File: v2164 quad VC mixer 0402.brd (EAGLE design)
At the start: 39.4 x 14.6 mm, 43 parts, among them IC1 TL072JD, IC2 TL072JD

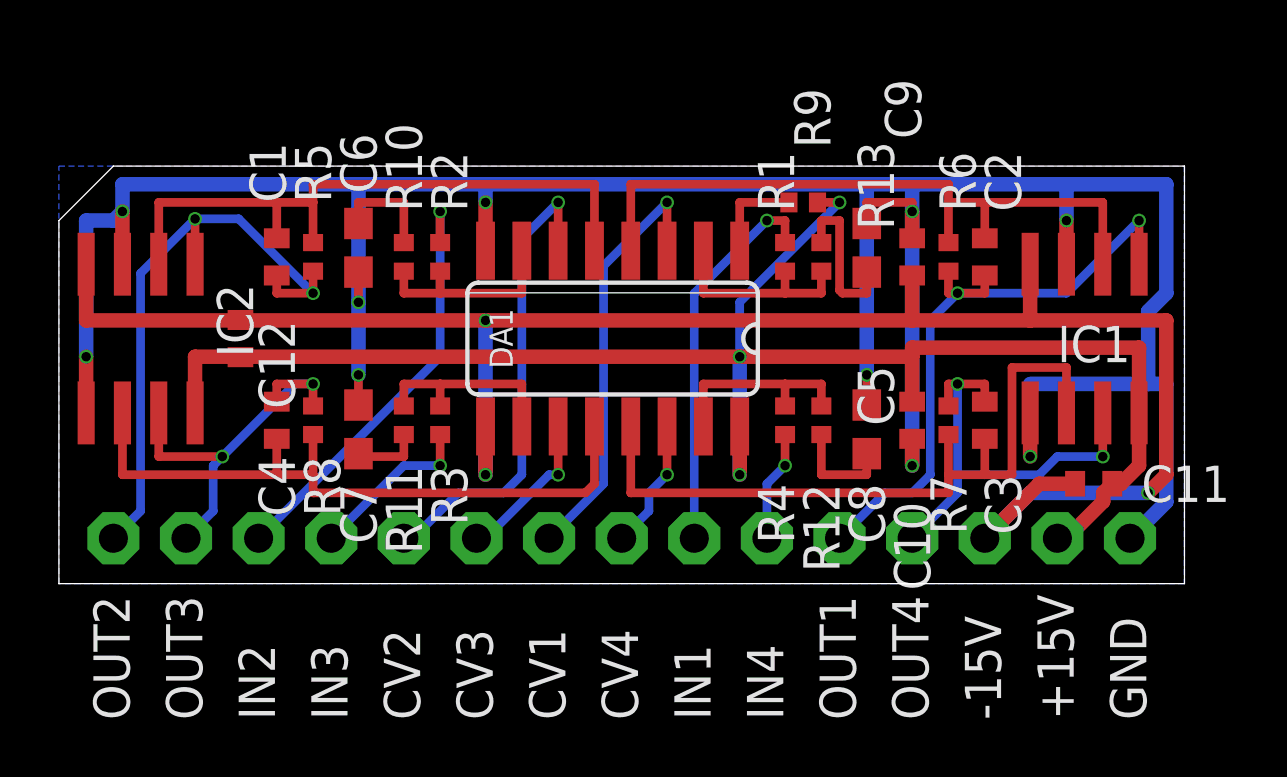
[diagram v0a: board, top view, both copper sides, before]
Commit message: Made mixer and added top labels
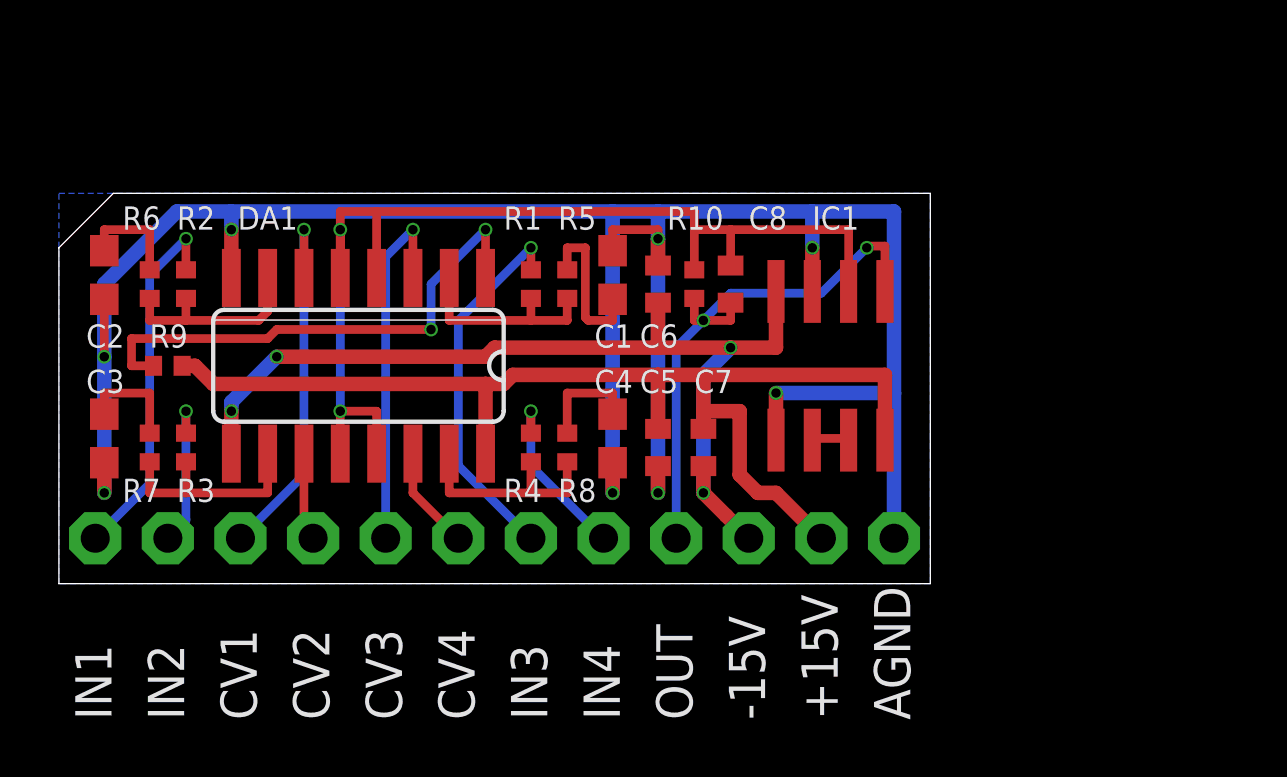
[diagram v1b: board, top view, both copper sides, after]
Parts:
- removed C10, C11, C12, C9: 100nF, rcl:C0402
- removed GND, OUT1, OUT2, OUT3, OUT4: (no value), joakim:MA01N-1J
- removed IC2: TL072JD, joakim:SO08J
- removed R11, R12: 500R, rcl:R0402
- removed R13: 7.5k for A, rcl:R0402
- added AGND, OUT: (no value), joakim:MA01N-1J
- C1, C2, C3, C4: value 100pF -> 560pF; device rcl:C0402 -> rcl:C0603
- C5, C6, C7: value 560pF -> 100nF; device rcl:C0603 -> rcl:C0402
- C8: value 560pF -> 100pF; device rcl:C0603 -> rcl:C0402
- R10: value 500R -> 30k
- R5, R6, R7, R8: value 30k -> 500R
- R9: value 500R -> 7.5k for A
- moved C2 30.8 mm to (1.59, 10.8), turned to 90 degrees
- moved C3 30.8 mm to (1.59, 5.08)
- moved R6 28.0 mm to (3.17, 10.5)
- moved R7 28.0 mm to (3.17, 4.76), turned to 270 degrees
- moved R9 23.2 mm to (3.81, 7.62), turned to 180 degrees
- moved IN1 21.0 mm to (1.27, 1.59)
- moved C7 12.1 mm to (22.5, 4.76), turned to 90 degrees
- moved C1 11.8 mm to (19.4, 10.8)
- moved C4 11.8 mm to (19.4, 5.08)
- moved CV1 10.8 mm to (6.35, 1.59)
- moved C6 10.6 mm to (21.0, 10.5)
- moved R10 10.2 mm to (22.2, 10.5)
- moved C5 10.1 mm to (21.0, 4.76), turned to 90 degrees
- moved DA1 8.94 mm to (10.5, 7.62)
- moved R2 8.94 mm to (4.45, 10.5)
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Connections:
- removed net CV3: CV3.1, DA1.11
- removed net N$3: C3.1, DA1.13, IC1.6, R7.1
- removed net N$7: C1.1, DA1.5, IC2.2, R5.1
- removed net OUT1: C2.2, IC1.1, OUT1.1, R6.2
- removed net OUT2: C1.2, IC2.1, OUT2.1, R5.2
- removed net OUT3: C4.2, IC2.7, OUT3.1, R8.2
- removed net OUT4: C3.2, IC1.7, OUT4.1, R7.2
- new net CV5: CV3.1, DA1.3
- new net OUT: C8.2, IC1.1, OUT.1, R10.2
- net +15V: now also C5.2, C7.2, R9.1; no longer C10.2, C11.2, C12.2, IC2.8, R13.1
- net -15V: now also C6.1, C7.1; no longer C11.1, C12.1, C9.1, IC2.4
- net CV1: now also DA1.6; no longer DA1.3
- net CV2: now also DA1.11; no longer DA1.6
- net GND: now also AGND.1, C1.1, C2.1, C3.1, C4.1, C6.2; no longer C10.1, C6.1, C7.1, C8.1, C9.2, GND.1, IC2.3, IC2.5
- net IN1: now also R2.1; no longer R1.1
- net IN2: now also R3.1; no longer R2.1
- net IN3: now also R1.1; no longer R3.1
- net N$1: now also IC1.6, IC1.7; no longer C4.1, DA1.12, IC2.6, R8.1
- net N$10: now also C2.2, R6.1; no longer C6.2, R10.1
- net N$11: now also C3.2, R7.1; no longer C7.2, R11.1
- net N$12: now also C4.2, R8.1; no longer C8.2, R12.1
- net N$17: now also R5.2; no longer R9.2
- net N$18: now also R6.2; no longer R10.2
- net N$19: now also R7.2; no longer R11.2
- net N$2: now also R9.2; no longer R13.2
- net N$20: now also R8.2; no longer R12.2
- net N$5: now also C8.1, DA1.12, DA1.13, DA1.5, R10.1; no longer C2.1, R6.1
- net N$9: now also C1.2, R5.1; no longer C5.2, R9.1
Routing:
- net -15V: track 67.0 -> 33.8 mm, vias 3 -> 4
- net N$3: track 26.2 -> 0.00 mm
- net N$7: track 23.0 -> 0.00 mm
- net N$1: track 24.1 -> 1.39 mm
- net OUT1: track 22.4 -> 0.00 mm, vias 2 -> 0
- net OUT2: track 21.8 -> 0.00 mm, vias 2 -> 0
- net OUT: track 0.00 -> 19.7 mm, vias 0 -> 2
- net +15V: track 58.5 -> 40.7 mm, vias 3 -> 0
- net GND: track 102.9 -> 86.6 mm, vias 10 -> 8
- net N$5: track 24.3 -> 40.2 mm, vias 0 -> 2
- net OUT4: track 15.6 -> 0.00 mm, vias 2 -> 0
- net N$2: track 3.41 -> 18.3 mm, vias 0 -> 2
- net OUT3: track 14.0 -> 0.00 mm, vias 2 -> 0
- net CV2: track 16.8 -> 3.09 mm, vias 1 -> 0
- net CV5: track 0.00 -> 12.9 mm, vias 0 -> 1
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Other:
- board size 39.4 x 14.6 mm -> 30.5 x 13.7 mm

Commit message: Finished top layer on both boards i think
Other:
- board text added: "3-20"
- board text added: "4VOB"
- board text added: "v1"
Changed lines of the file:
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@@
 <wire x1="30.48" y1="13.6525" x2="30.48" y2="0" width="0" layer="20"/>
 <wire x1="30.48" y1="0" x2="0" y2="0" width="0" layer="20"/>
+<text x="28.575" y="3.81" size="1.016" layer="25" font="vector" rot="R180">4VOB</text>
+<text x="11.43" y="12.3825" size="0.8128" layer="25" font="vector">3-20</text>
+<text x="28.8925" y="12.3825" size="0.8128" layer="25" font="vector">v1</text>
 </plain>
 <attributes>

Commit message: Completed silkscreen and routing on both vca and mixer.
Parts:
- added U$1: (no value), joakim:XONIK_LOGO_20
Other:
- board text added: "+15v"
- board text added: "-15v"
- board text added: "4ch exp mixer"
- board text added: "AGND"
- board text added: "C1"
- board text added: "C2"
- board text added: "C3"
- board text added: "C4"
- board text added: "I1"
- board text added: "I2"
- board text added: "I3"
- board text added: "I4"
- board text added: "O"
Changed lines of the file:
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@@
 <layer number="2" name="Route2" color="16" fill="1" visible="no" active="no"/>
 <layer number="15" name="Route15" color="23" fill="1" visible="no" active="no"/>
-<layer number="16" name="Bottom" color="1" fill="1" visible="yes" active="yes"/>
+<layer number="16" name="Bottom" color="1" fill="1" visible="no" active="yes"/>
 <layer number="17" name="Pads" color="2" fill="1" visible="yes" active="yes"/>
 <layer number="18" name="Vias" color="2" fill="1" visible="yes" active="yes"/>
@@
 <layer number="20" name="Dimension" color="24" fill="1" visible="yes" active="yes"/>
 <layer number="21" name="tPlace" color="7" fill="1" visible="yes" active="yes"/>
-<layer number="22" name="bPlace" color="7" fill="1" visible="yes" active="yes"/>
+<layer number="22" name="bPlace" color="7" fill="1" visible="no" active="yes"/>
 <layer number="23" name="tOrigins" color="15" fill="1" visible="yes" active="yes"/>
-<layer number="24" name="bOrigins" color="15" fill="1" visible="yes" active="yes"/>
+<layer number="24" name="bOrigins" color="15" fill="1" visible="no" active="yes"/>
 <layer number="25" name="tNames" color="7" fill="1" visible="yes" active="yes"/>
-<layer number="26" name="bNames" color="7" fill="1" visible="yes" active="yes"/>
+<layer number="26" name="bNames" color="7" fill="1" visible="no" active="yes"/>
 <layer number="27" name="tValues" color="7" fill="1" visible="no" active="yes"/>
 <layer number="28" name="bValues" color="7" fill="1" visible="no" active="yes"/>
@@
 <layer number="38" name="bTest" color="7" fill="1" visible="no" active="yes"/>
 <layer number="39" name="tKeepout" color="4" fill="11" visible="yes" active="yes"/>
-<layer number="40" name="bKeepout" color="1" fill="11" visible="yes" active="yes"/>
+<layer number="40" name="bKeepout" color="1" fill="11" visible="no" active="yes"/>
 <layer number="41" name="tRestrict" color="4" fill="10" visible="yes" active="yes"/>
-<layer number="42" name="bRestrict" color="1" fill="10" visible="yes" active="yes"/>
+<layer number="42" name="bRestrict" color="1" fill="10" visible="no" active="yes"/>
 <layer number="43" name="vRestrict" color="2" fill="10" visible="no" active="yes"/>
 <layer number="44" name="Drills" color="7" fill="1" visible="no" active="yes"/>
@@
 <layer number="50" name="dxf" color="7" fill="1" visible="no" active="no"/>
 <layer number="51" name="tDocu" color="7" fill="1" visible="yes" active="yes"/>
-<layer number="52" name="bDocu" color="7" fill="1" visible="yes" active="yes"/>
+<layer number="52" name="bDocu" color="7" fill="1" visible="no" active="yes"/>
 <layer number="53" name="tGND_GNDA" color="7" fill="9" visible="no" active="no"/>
 <layer number="54" name="bGND_GNDA" color="1" fill="9" visible="no" active="no"/>
@@
 <text x="11.43" y="12.3825" size="0.8128" layer="25" font="vector">3-20</text>
 <text x="28.8925" y="12.3825" size="0.8128" layer="25" font="vector">v1</text>
+<text x="0.635" y="3.4925" size="1.27" layer="26" font="vector" rot="MR90">I1</text>
+<text x="3.175" y="3.4925" size="1.27" layer="26" font="vector" rot="MR90">I2</text>
+<text x="5.715" y="3.4925" size="1.27" layer="26" font="vector" rot="MR90">C1</text>
+<text x="8.255" y="3.4925" size="1.27" layer="26" font="vector" rot="MR90">C2</text>
+<text x="10.795" y="3.4925" size="1.27" layer="26" font="vector" rot="MR90">C3</text>
+<text x="13.335" y="3.4925" size="1.27" layer="26" font="vector" rot="MR90">C4</text>
+<text x="15.875" y="3.4925" size="1.27" layer="26" font="vector" rot="MR90">I3</text>
+<text x="18.415" y="3.4925" size="1.27" layer="26" font="vector" rot="MR90">I4</text>
+<text x="20.955" y="3.4925" size="1.27" layer="26" font="vector" rot="MR90">O</text>
+<text x="23.495" y="3.4925" size="1.27" layer="26" font="vector" rot="MR90">-15v</text>
+<text x="26.035" y="3.4925" size="1.27" layer="26" font="vector" rot="MR90">+15v</text>
+<text x="28.575" y="3.4925" size="1.27" layer="26" font="vector" rot="MR90">AGND</text>
+<text x="17.145" y="6.35" size="1.27" layer="26" font="vector" rot="MR0">4ch exp mixer</text>
 </plain>
 <attributes>
@@
 </element>
 <element name="CV3" library="joakim" package="MA01N-1J" value="" x="11.43" y="1.5875" smashed="yes" rot="R90">
-<attribute name="NAME" x="12.0015" y="-4.7625" size="1.27" layer="25" ratio="10" rot="R90"/>
 <attribute name="VALUE" x="14.351" y="-0.9525" size="1.27" layer="27" ratio="10" rot="R90"/>
 </element>
 <element name="CV1" library="joakim" package="MA01N-1J" value="" x="6.35" y="1.5875" smashed="yes" rot="R90">
-<attribute name="NAME" x="6.9215" y="-4.7625" size="1.27" layer="25" ratio="10" rot="R90"/>
 <attribute name="VALUE" x="9.271" y="-0.9525" size="1.27" layer="27" ratio="10" rot="R90"/>
 </element>
 <element name="CV2" library="joakim" package="MA01N-1J" value="" x="8.89" y="1.5875" smashed="yes" rot="R90">
-<attribute name="NAME" x="9.4615" y="-4.7625" size="1.27" layer="25" ratio="10" rot="R90"/>
 <attribute name="VALUE" x="11.811" y="-0.9525" size="1.27" layer="27" ratio="10" rot="R90"/>
 </element>
 <element name="CV4" library="joakim" package="MA01N-1J" value="" x="13.97" y="1.5875" smashed="yes" rot="R90">
-<attribute name="NAME" x="14.5415" y="-4.7625" size="1.27" layer="25" ratio="10" rot="R90"/>
 <attribute name="VALUE" x="16.891" y="-0.9525" size="1.27" layer="27" ratio="10" rot="R90"/>
 </element>
 <element name="IN3" library="joakim" package="MA01N-1J" value="" x="16.51" y="1.5875" smashed="yes" rot="R90">
-<attribute name="NAME" x="17.0815" y="-4.7625" size="1.27" layer="25" ratio="10" rot="R90"/>
 <attribute name="VALUE" x="19.431" y="-0.9525" size="1.27" layer="27" ratio="10" rot="R90"/>
 </element>
 <element name="IN1" library="joakim" package="MA01N-1J" value="" x="1.27" y="1.5875" smashed="yes" rot="R90">
-<attribute name="NAME" x="1.8415" y="-4.7625" size="1.27" layer="25" ratio="10" rot="R90"/>
 <attribute name="VALUE" x="4.191" y="-0.9525" size="1.27" layer="27" ratio="10" rot="R90"/>
 </element>
 <element name="IN2" library="joakim" package="MA01N-1J" value="" x="3.81" y="1.5875" smashed="yes" rot="R90">
-<attribute name="NAME" x="4.3815" y="-4.7625" size="1.27" layer="25" ratio="10" rot="R90"/>
 <attribute name="VALUE" x="6.731" y="-0.9525" size="1.27" layer="27" ratio="10" rot="R90"/>
 </element>
 <element name="IN4" library="joakim" package="MA01N-1J" value="" x="19.05" y="1.5875" smashed="yes" rot="R90">
-<attribute name="NAME" x="19.6215" y="-4.7625" size="1.27" layer="25" ratio="10" rot="R90"/>
 <attribute name="VALUE" x="21.971" y="-0.9525" size="1.27" layer="27" ratio="10" rot="R90"/>
 </element>
 <element name="OUT" library="joakim" package="MA01N-1J" value="" x="21.59" y="1.5875" smashed="yes" rot="R90">
-<attribute name="NAME" x="22.1615" y="-4.7625" size="1.27" layer="25" ratio="10" rot="R90"/>
 <attribute name="VALUE" x="24.511" y="-0.9525" size="1.27" layer="27" ratio="10" rot="R90"/>
 </element>
@@
 </element>
 <element name="+15V" library="joakim" package="MA01N-1J" value="" x="26.67" y="1.5875" smashed="yes" rot="R90">
-<attribute name="NAME" x="27.2415" y="-4.7625" size="1.27" layer="25" ratio="10" rot="R90"/>
 <attribute name="VALUE" x="29.591" y="-0.9525" size="1.27" layer="27" ratio="10" rot="R90"/>
 </element>
 <element name="AGND" library="joakim" package="MA01N-1J" value="" x="29.21" y="1.5875" smashed="yes" rot="R90">
-<attribute name="NAME" x="29.7815" y="-4.7625" size="1.27" layer="25" ratio="10" rot="R90"/>
 <attribute name="VALUE" x="32.131" y="-0.9525" size="1.27" layer="27" ratio="10" rot="R90"/>
 </element>
 <element name="-15V" library="joakim" package="MA01N-1J" value="" x="24.13" y="1.5875" smashed="yes" rot="R90">
-<attribute name="NAME" x="24.7015" y="-4.7625" size="1.27" layer="25" ratio="10" rot="R90"/>
 <attribute name="VALUE" x="27.051" y="-0.9525" size="1.27" layer="27" ratio="10" rot="R90"/>
 </element>
@@
 <attribute name="VALUE" x="23.0505" y="9.525" size="1.27" layer="27" rot="R270"/>
 </element>
+<element name="U$1" library="joakim" package="XONIK_LOGO_20" value="" x="21.59" y="7.9375" smashed="yes" rot="MR0"/>
 </elements>
 <signals>
